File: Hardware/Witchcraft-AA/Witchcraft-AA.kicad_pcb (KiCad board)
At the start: 2 copper layers, 180 x 81 mm, 21 parts, among them J0 USB_C_Molex_201267-0005, J1 USB_C_Molex_201267-0005, J3 Conn_Power_Coax_IBM_hanging_M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, J4 Molex_0015913074, U1 Z1 extreme, U2 LM26420-Q1xx-xxxx

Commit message: Started working on custom buttons for the shell.
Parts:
- removed J3: Conn_Power_Coax_IBM_hanging_MountingPin, LRJ:Jack_IBM_Coax_Power_5.55x7.5mm_Hanging
- removed J4: Molex_0015913074, LRJ:Molex_70634_15913074_1x07-2MP_P2.54mm_Vertical
- added J2: TE_2129567-1, LRJ:TE_2129567-1, F.Cu at (33.2, 32.8)
- moved BT1 177.4 mm to (-29.3, 4.19)
- moved C1 177.4 mm to (5.74, 26.9)
- moved C2 177.4 mm to (17.2, 28.5)
- moved C3 177.4 mm to (16.8, 19.7)
- moved C4 177.4 mm to (23.4, 26.7)
- moved C5 177.4 mm to (20.8, 19.7)
- moved C6 177.4 mm to (12.5, 26.9)
- moved C7 177.4 mm to (24.3, -28.6)
- moved C8 177.4 mm to (24.9, -30.8)
- moved C9 177.4 mm to (29.7, -30.8)
- moved D1 177.4 mm to (12.7, -33.4)
- moved F1 177.4 mm to (17.1, -27.4)
- moved J0 177.4 mm to (7.34, 36.5)
- moved J1 177.4 mm to (18.6, 36.5)
- moved R1 177.4 mm to (15.2, 30.9)
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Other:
- outline, holes or cut-outs redrawn

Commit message: Some chances to start/rectangle-buttons in mech, and startedmaking the M.2 ports.
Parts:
- removed R3: R_ERJ-3GEYJ105V, Resistor_SMD:R_0603_1608Metric
- added J3: Conn_01x05_Socket, Connector_PinHeader_1.27mm:PinHeader_1x05_P1.27mm_Vertical_SMD_Pin1Left, F.Cu at (48.1, 31.3)
- added U3: K3LKCKC0BM, LRJ:SAMSUNG_FBGA-315_12x14mm_Layout23x23_P0.5mmP0.65mm, F.Cu at (32.2, 14.8)
- added U4: K3LKCKC0BM, LRJ:SAMSUNG_FBGA-315_12x14mm_Layout23x23_P0.5mmP0.65mm, F.Cu at (45.9, 14.8)
- added U_A1: Hall_Sensor, Package_TO_SOT_SMD:SOT-23-3, F.Cu at (72.9, -19.2)
- added U_B2: Hall_Sensor, Package_TO_SOT_SMD:SOT-23-3, F.Cu at (67.5, -19.2)
- added U_D1: Hall_Sensor, Package_TO_SOT_SMD:SOT-23-3, F.Cu at (-82.2, -23.4)
- added U_D2: Hall_Sensor, Package_TO_SOT_SMD:SOT-23-3, F.Cu at (-82.4, -16.0)
- added U_D3: Hall_Sensor, Package_TO_SOT_SMD:SOT-23-3, F.Cu at (-87.2, -19.8)
- added U_D4: Hall_Sensor, Package_TO_SOT_SMD:SOT-23-3, F.Cu at (-77.4, -19.6)
- added U_H8: Hall_Sensor, Package_TO_SOT_SMD:SOT-23-3, F.Cu at (58.0, 33.8)
- added U_M13: Hall_Sensor, Package_TO_SOT_SMD:SOT-23-3, F.Cu at (-57.1, 33.5)
- added U_S1: Hall_Sensor, Package_TO_SOT_SMD:SOT-23-3, F.Cu at (55.0, -34.6)
- added U_S5: Hall_Sensor, Package_TO_SOT_SMD:SOT-23-3, F.Cu at (-46.0, -34.4)
- added U_X10: Hall_Sensor, Package_TO_SOT_SMD:SOT-23-3, F.Cu at (67.4, -25.4)
- added U_Y11: Hall_Sensor, Package_TO_SOT_SMD:SOT-23-3, F.Cu at (72.7, -25.4)
- moved J0 90.4 mm to (86.0, -8.00), turned to 90 degrees
- moved C6 76.2 mm to (79.4, -9.60), turned to 90 degrees
- moved J1 18.4 mm to (0.20, 36.5)
- moved U2 12.3 mm to (16.3, 20.3)
- moved BT1 10.9 mm to (-38.7, -1.34), turned to -90 degrees
- moved C3 9.21 mm to (7.60, 20.2)
- moved C5 9.21 mm to (11.6, 20.2)
- moved F1 6.90 mm to (16.2, -34.2)
- moved U1 6.50 mm to (35.4, -7.20)
- moved C7 4.83 mm to (22.3, -33.0)
- moved D1 4.83 mm to (10.7, -37.8)
- moved C8 4.83 mm to (22.9, -35.2)
- moved C9 4.83 mm to (27.7, -35.2)
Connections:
- U2 pad 10: unconnected-(U2-SW2-Pad10) -> +1V8
- U2 pad 3: unconnected-(U2-SW1-Pad3) -> +3.3V
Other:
- outline, holes or cut-outs redrawn

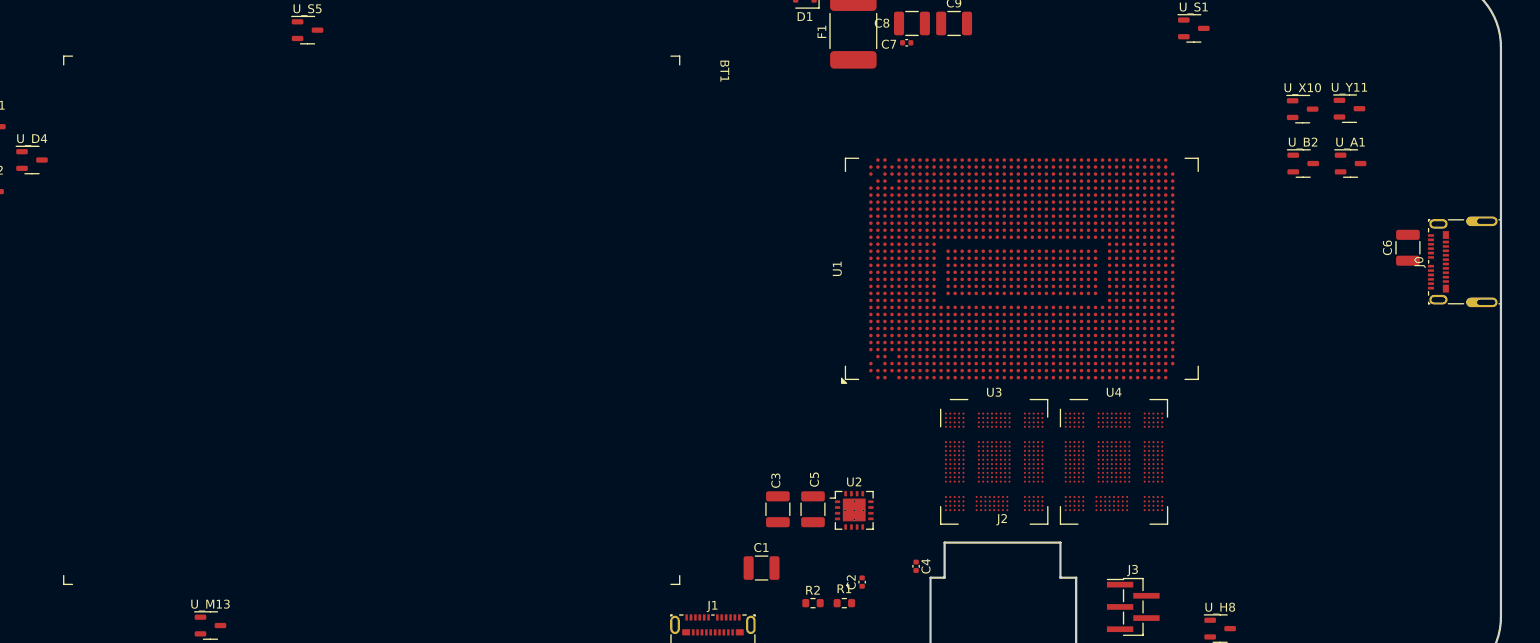
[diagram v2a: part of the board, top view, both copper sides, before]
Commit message: added some reference-pictures for tracking down a suitable cooling-solution.
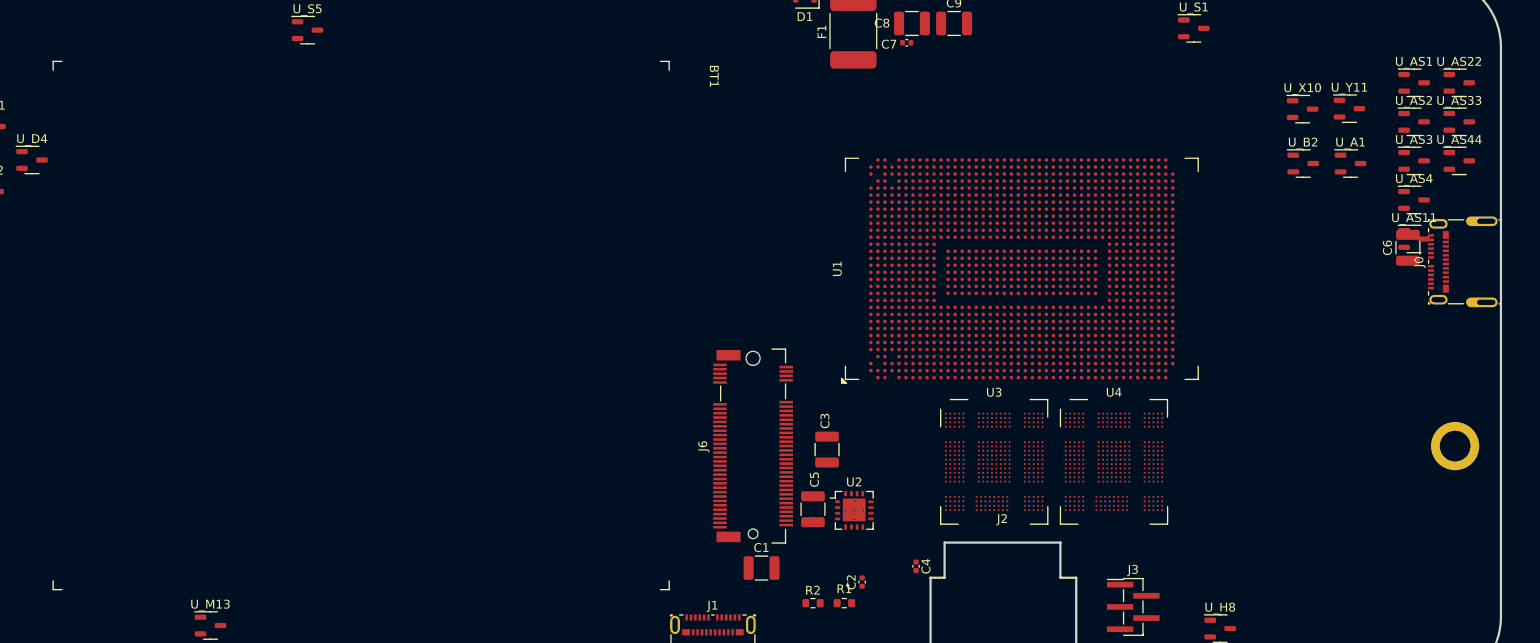
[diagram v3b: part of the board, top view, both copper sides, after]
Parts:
- added J6: 10157930, LRJ:Amphenol_10157930_PCI_Express_M.2_2280_less-court, F.Cu at (4.78, 13.0)
- added U_AS1: Hall_Sensor, Package_TO_SOT_SMD:SOT-23-3, F.Cu at (80.1, -28.4)
- added U_AS11: Hall_Sensor, Package_TO_SOT_SMD:SOT-23-3, F.Cu at (80.1, -10.6)
- added U_AS2: Hall_Sensor, Package_TO_SOT_SMD:SOT-23-3, F.Cu at (80.1, -23.9)
- added U_AS22: Hall_Sensor, Package_TO_SOT_SMD:SOT-23-3, F.Cu at (85.2, -28.4)
- added U_AS3: Hall_Sensor, Package_TO_SOT_SMD:SOT-23-3, F.Cu at (80.1, -19.5)
- added U_AS33: Hall_Sensor, Package_TO_SOT_SMD:SOT-23-3, F.Cu at (85.2, -23.9)
- added U_AS4: Hall_Sensor, Package_TO_SOT_SMD:SOT-23-3, F.Cu at (80.1, -15.1)
- added U_AS44: Hall_Sensor, Package_TO_SOT_SMD:SOT-23-3, F.Cu at (85.2, -19.5)
- moved C3 8.81 mm to (13.2, 13.4)
- moved BT1 1.34 mm to (-39.9, -0.74)
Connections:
- U3 pad B12: Net-(U3E-VSS-PadB12) -> GND
- U3 pad B2: Net-(U3E-VSS-PadB12) -> GND
- U3 pad B5: Net-(U3E-VSS-PadB12) -> GND
- U3 pad B6: Net-(U3E-VSS-PadB12) -> GND
- U3 pad C3: Net-(U3E-VSS-PadB12) -> GND
- U3 pad C5: Net-(U3E-VSS-PadB12) -> GND
- U3 pad C6: Net-(U3E-VSS-PadB12) -> GND
- U3 pad D12: Net-(U3E-VSS-PadB12) -> GND
- U3 pad D3: Net-(U3E-VSS-PadB12) -> GND
- U3 pad E4: Net-(U3E-VSS-PadB12) -> GND
- U3 pad E5: Net-(U3E-VSS-PadB12) -> GND
- U3 pad E6: Net-(U3E-VSS-PadB12) -> GND
- U3 pad F12: Net-(U3E-VSS-PadB12) -> GND
- U3 pad F4: Net-(U3E-VSS-PadB12) -> GND
- U3 pad F5: Net-(U3E-VSS-PadB12) -> GND
- U3 pad F6: Net-(U3E-VSS-PadB12) -> GND
- U3 pad G3: Net-(U3E-VSS-PadB12) -> GND
- U3 pad G4: Net-(U3E-VSS-PadB12) -> GND
- U3 pad G6: Net-(U3E-VSS-PadB12) -> GND
- U3 pad G9: Net-(U3E-VSS-PadB12) -> GND
- U3 pad H10: Net-(U3E-VSS-PadB12) -> GND
- U3 pad H2: Net-(U3E-VSS-PadB12) -> GND
- U3 pad J12: Net-(U3E-VSS-PadB12) -> GND
- U3 pad J4: Net-(U3E-VSS-PadB12) -> GND
- U3 pad K10: Net-(U3E-VSS-PadB12) -> GND
- U3 pad K2: Net-(U3E-VSS-PadB12) -> GND
- U3 pad L6: Net-(U3E-VSS-PadB12) -> GND
- U3 pad L9: Net-(U3E-VSS-PadB12) -> GND
- U3 pad M12: Net-(U3E-VSS-PadB12) -> GND
- U3 pad M4: Net-(U3E-VSS-PadB12) -> GND
- U3 pad M5: Net-(U3E-VSS-PadB12) -> GND
- U3 pad M6: Net-(U3E-VSS-PadB12) -> GND
- U3 pad N4: Net-(U3E-VSS-PadB12) -> GND
- U3 pad N5: Net-(U3E-VSS-PadB12) -> GND
- U3 pad N6: Net-(U3E-VSS-PadB12) -> GND
- U3 pad P12: Net-(U3E-VSS-PadB12) -> GND
- U3 pad P3: Net-(U3E-VSS-PadB12) -> GND
- U3 pad R4: Net-(U3E-VSS-PadB12) -> GND
- U3 pad R5: Net-(U3E-VSS-PadB12) -> GND
- U3 pad R6: Net-(U3E-VSS-PadB12) -> GND
- U3 pad T12: Net-(U3E-VSS-PadB12) -> GND
- U3 pad T2: Net-(U3E-VSS-PadB12) -> GND
- U3 pad T3: Net-(U3E-VSS-PadB12) -> GND
- U3 pad T4: Net-(U3E-VSS-PadB12) -> GND
- U3 pad T5: Net-(U3E-VSS-PadB12) -> GND
- U3 pad T6: Net-(U3E-VSS-PadB12) -> GND
- U4 pad B12: Net-(U4E-VSS-PadB12) -> GND
- U4 pad B2: Net-(U4E-VSS-PadB12) -> GND
- U4 pad B5: Net-(U4E-VSS-PadB12) -> GND
- U4 pad B6: Net-(U4E-VSS-PadB12) -> GND
- U4 pad C3: Net-(U4E-VSS-PadB12) -> GND
- U4 pad C5: Net-(U4E-VSS-PadB12) -> GND
- U4 pad C6: Net-(U4E-VSS-PadB12) -> GND
- U4 pad D12: Net-(U4E-VSS-PadB12) -> GND
- U4 pad D3: Net-(U4E-VSS-PadB12) -> GND
- U4 pad E4: Net-(U4E-VSS-PadB12) -> GND
- U4 pad E5: Net-(U4E-VSS-PadB12) -> GND
- U4 pad E6: Net-(U4E-VSS-PadB12) -> GND
- U4 pad F12: Net-(U4E-VSS-PadB12) -> GND
- U4 pad F4: Net-(U4E-VSS-PadB12) -> GND
- U4 pad F5: Net-(U4E-VSS-PadB12) -> GND
- U4 pad F6: Net-(U4E-VSS-PadB12) -> GND
- U4 pad G3: Net-(U4E-VSS-PadB12) -> GND
- U4 pad G4: Net-(U4E-VSS-PadB12) -> GND
- U4 pad G6: Net-(U4E-VSS-PadB12) -> GND
- U4 pad G9: Net-(U4E-VSS-PadB12) -> GND
- U4 pad H10: Net-(U4E-VSS-PadB12) -> GND
- U4 pad H2: Net-(U4E-VSS-PadB12) -> GND
- U4 pad J12: Net-(U4E-VSS-PadB12) -> GND
- U4 pad J4: Net-(U4E-VSS-PadB12) -> GND
- U4 pad K10: Net-(U4E-VSS-PadB12) -> GND
- U4 pad K2: Net-(U4E-VSS-PadB12) -> GND
- U4 pad L6: Net-(U4E-VSS-PadB12) -> GND
- U4 pad L9: Net-(U4E-VSS-PadB12) -> GND
- U4 pad M12: Net-(U4E-VSS-PadB12) -> GND
- U4 pad M4: Net-(U4E-VSS-PadB12) -> GND
- U4 pad M5: Net-(U4E-VSS-PadB12) -> GND
- U4 pad M6: Net-(U4E-VSS-PadB12) -> GND
- U4 pad N4: Net-(U4E-VSS-PadB12) -> GND
- U4 pad N5: Net-(U4E-VSS-PadB12) -> GND
- U4 pad N6: Net-(U4E-VSS-PadB12) -> GND
- U4 pad P12: Net-(U4E-VSS-PadB12) -> GND
- U4 pad P3: Net-(U4E-VSS-PadB12) -> GND
- U4 pad R4: Net-(U4E-VSS-PadB12) -> GND
- U4 pad R5: Net-(U4E-VSS-PadB12) -> GND
- U4 pad R6: Net-(U4E-VSS-PadB12) -> GND
- U4 pad T12: Net-(U4E-VSS-PadB12) -> GND
- U4 pad T2: Net-(U4E-VSS-PadB12) -> GND
- U4 pad T3: Net-(U4E-VSS-PadB12) -> GND
- U4 pad T4: Net-(U4E-VSS-PadB12) -> GND
- U4 pad T5: Net-(U4E-VSS-PadB12) -> GND
- U4 pad T6: Net-(U4E-VSS-PadB12) -> GND

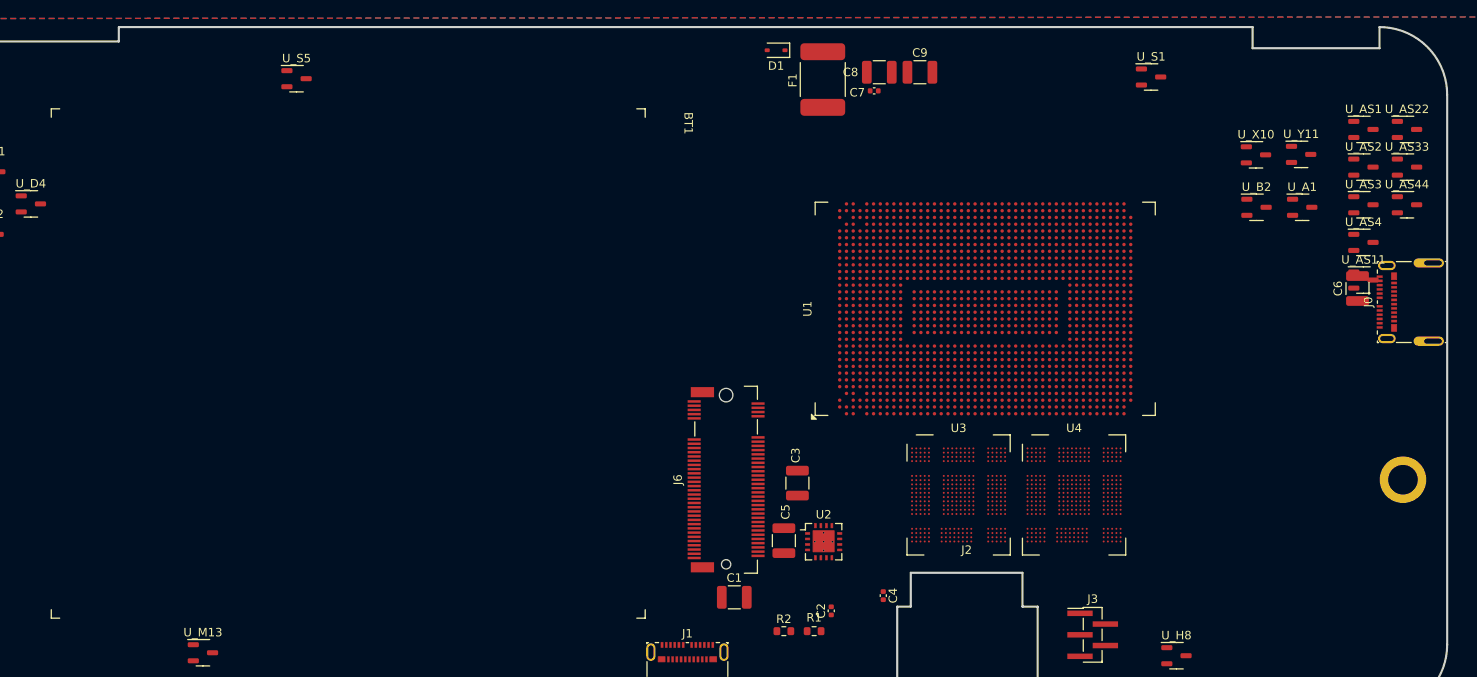
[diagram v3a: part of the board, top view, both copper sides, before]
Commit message: Almost completed the design of the new finstack, and have begun work on a redesign of cold-plate and rearrangement of components
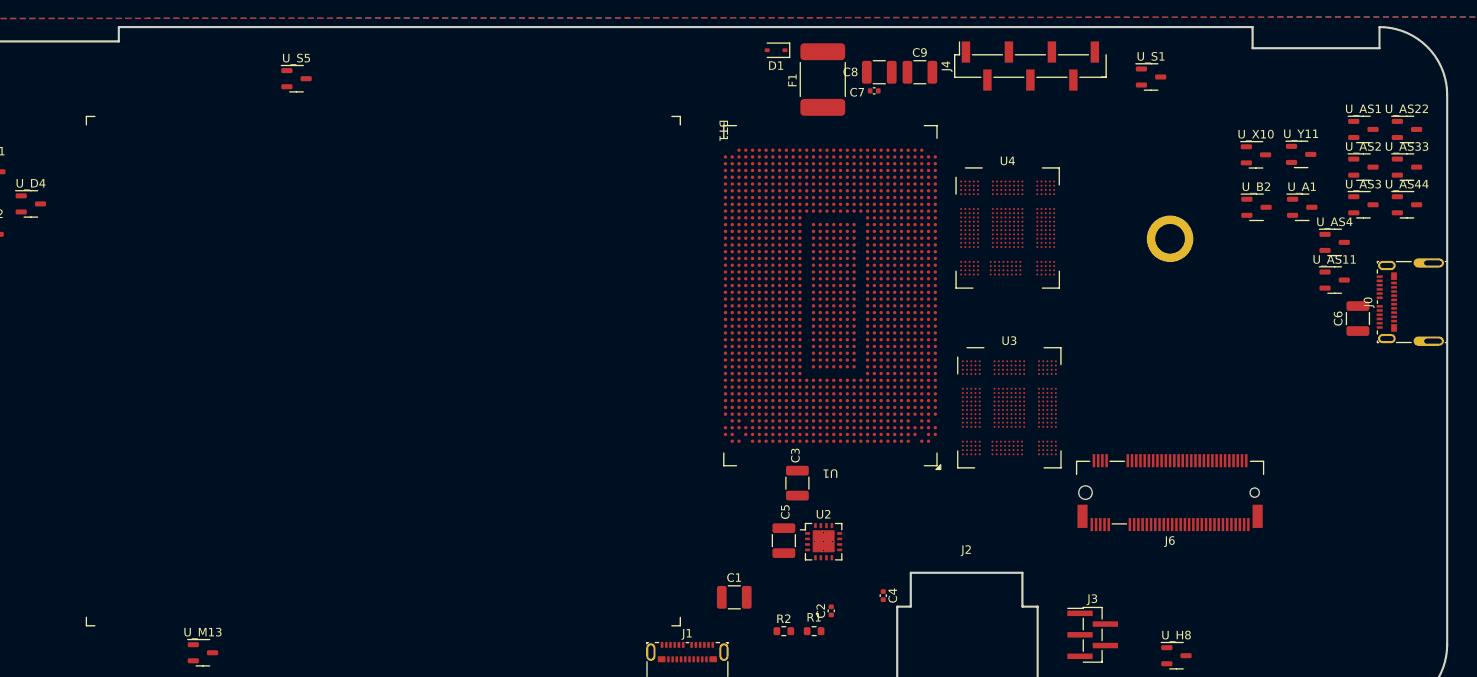
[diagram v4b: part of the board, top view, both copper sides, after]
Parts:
- added J4: Conn_NREC007, Connector_PinHeader_2.54mm:PinHeader_1x07_P2.54mm_Vertical_SMD_Pin1Right, F.Cu at (40.7, -35.9)
- J6: footprint LRJ:Amphenol_10157930_PCI_Express_M.2_2280_less-court -> LRJ:Amphenol_10157930_PCI_Express_M.2_2230_less-court
- moved J6 52.5 mm to (57.2, 14.5), turned to 0 degrees
- moved U4 32.5 mm to (38.0, -16.8)
- moved U1 18.4 mm to (17.1, -8.75), turned to 180 degrees
- moved U3 11.9 mm to (38.2, 4.50)
- moved BT1 4.25 mm to (-35.7, 0.16)
- moved C6 3.55 mm to (79.5, -6.05)
- moved U_AS11 3.40 mm to (76.7, -10.6)
- moved U_AS4 3.40 mm to (76.7, -15.1)
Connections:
- J0 pad A6: unconnected-(J0-D+-PadA6) -> /USB/USB2_D+
- J0 pad A7: unconnected-(J0-D--PadA7) -> /USB/USB2_D-
- U1 pad AP3: unconnected-(U1A-TDI-PadAP3) -> Net-(J4-Pin_3)
- U1 pad AR2: unconnected-(U1A-TCK-PadAR2) -> Net-(J4-Pin_4)
- U1 pad AT2: unconnected-(U1A-~{DBREQ}-PadAT2) -> Net-(J4-Pin_6)
- U1 pad AU1: unconnected-(U1A-TDO-PadAU1) -> Net-(J4-Pin_7)
- U1 pad AU3: unconnected-(U1A-TMS-PadAU3) -> Net-(J4-Pin_5)

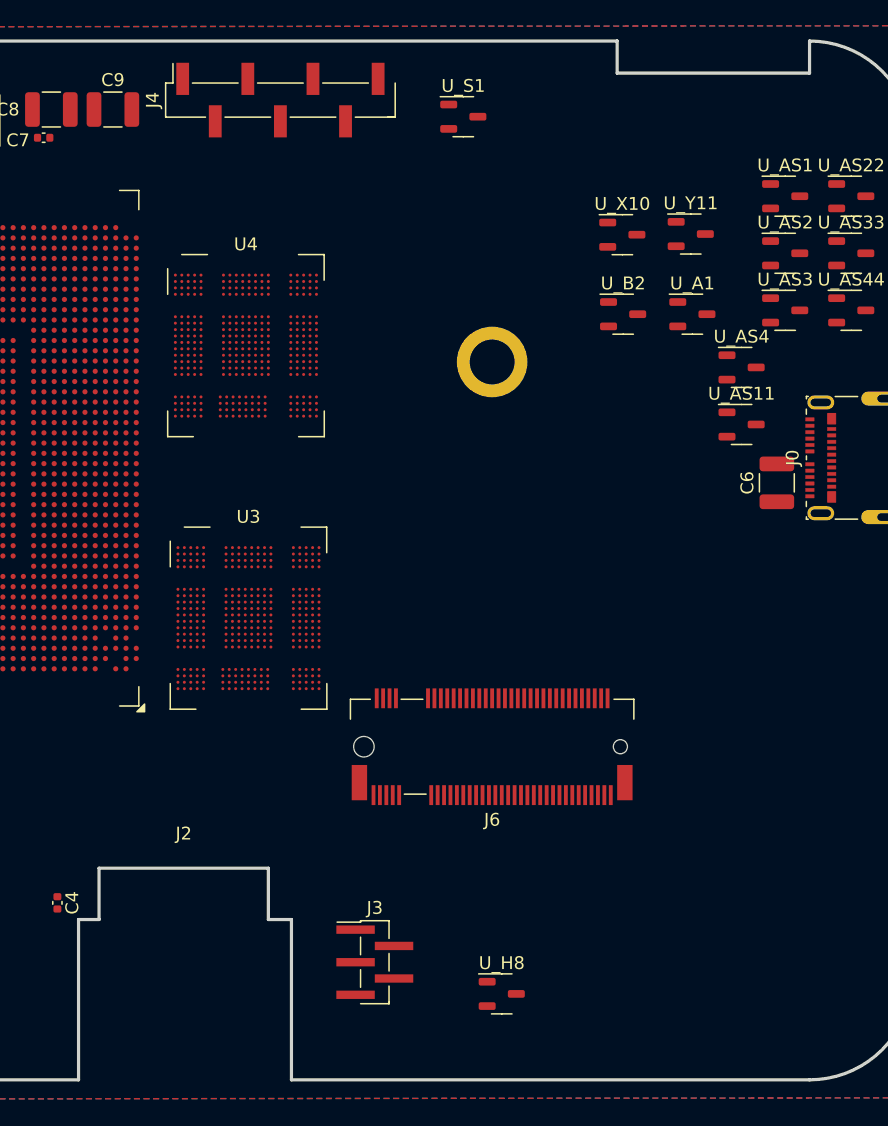
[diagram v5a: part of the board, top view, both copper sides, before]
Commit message: Upgraded the shell-assembly to the Assembly4 workbench, allowing for better performance.
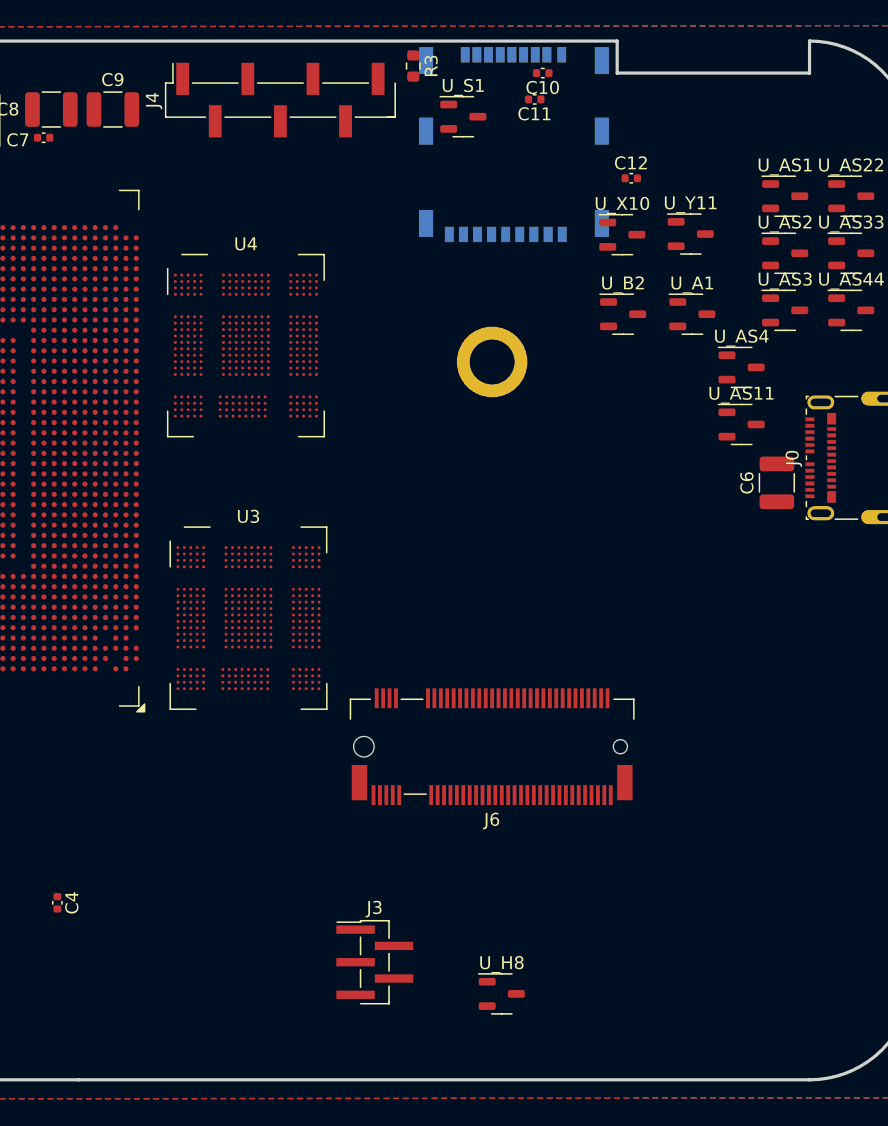
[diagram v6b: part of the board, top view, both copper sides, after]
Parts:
- removed J2: TE_2129567-1, LRJ:TE_2129567-1
- added C10: C_CGA2B1X7R1V224K, Capacitor_SMD:C_0402_1005Metric, F.Cu at (61.2, -38.0)
- added C11: C_CGA2B1X7R1V224K, Capacitor_SMD:C_0402_1005Metric, F.Cu at (60.6, -36.0)
- added C12: C_CGA2B1X7R1V224K, Capacitor_SMD:C_0402_1005Metric, F.Cu at (68.1, -29.8)
- added J7: Amphenol_101019966912A, LRJ:microSD_HC_Amphenol_101019966912A, B.Cu at (59.0, -32.6)
- added R3: R_ERJ-3GEYJ105V, Resistor_SMD:R_0603_1608Metric, F.Cu at (51.1, -38.5)
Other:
- outline, holes or cut-outs redrawn
